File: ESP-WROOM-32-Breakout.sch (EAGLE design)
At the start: 10 parts, among them SW1 PROG, SW2 RST, U3 ESP-WROOM-32

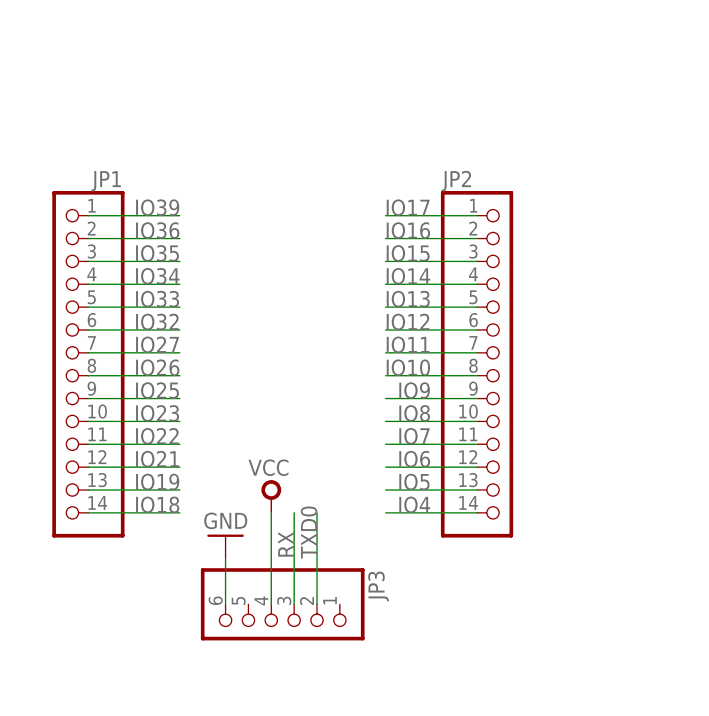
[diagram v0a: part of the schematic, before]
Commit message: smaller header pads reduced board size added mounting holes stitching via’s at antenna
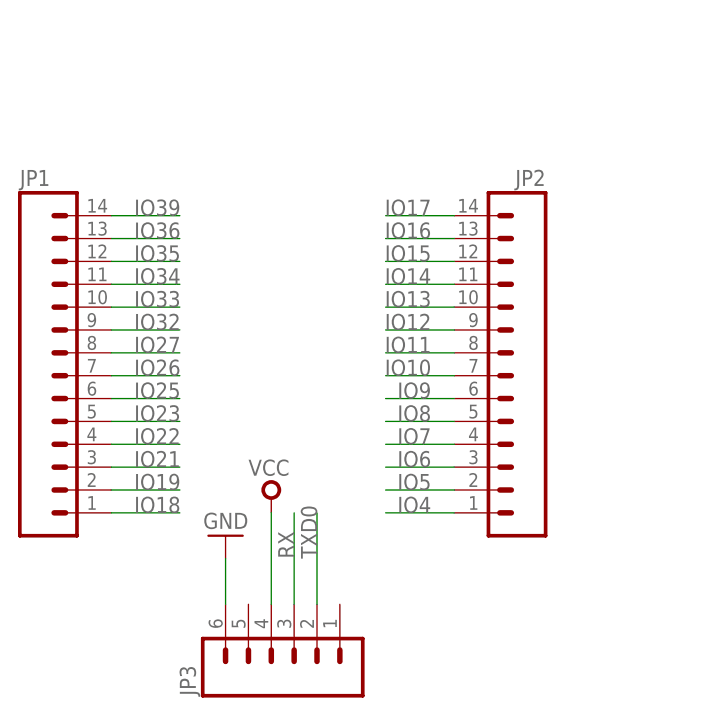
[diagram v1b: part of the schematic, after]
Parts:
- JP1, JP2: device pinhead:PINHD-1X14 -> SparkFun-Connectors:M14
- JP3: device pinhead:PINHD-1X6 -> SparkFun-Connectors:M06SILK_FEMALE_PTH
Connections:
- net IO10: now also JP2.7; no longer JP2.8
- net IO11: now also JP2.8; no longer JP2.7
- net IO12: now also JP2.9; no longer JP2.6
- net IO13: now also JP2.10; no longer JP2.5
- net IO14: now also JP2.11; no longer JP2.4
- net IO15: now also JP2.12; no longer JP2.3
- net IO16: now also JP2.13; no longer JP2.2
- net IO17: now also JP2.14; no longer JP2.1
- net IO18: now also JP1.1; no longer JP1.14
- net IO19: now also JP1.2; no longer JP1.13
- net IO21: now also JP1.3; no longer JP1.12
- net IO22: now also JP1.4; no longer JP1.11
- net IO23: now also JP1.5; no longer JP1.10
- net IO25: now also JP1.6; no longer JP1.9
- net IO26: now also JP1.7; no longer JP1.8
- net IO27: now also JP1.8; no longer JP1.7
- net IO32: now also JP1.9; no longer JP1.6
- net IO33: now also JP1.10; no longer JP1.5
- net IO34: now also JP1.11; no longer JP1.4
- net IO35: now also JP1.12; no longer JP1.3
- net IO36: now also JP1.13; no longer JP1.2
- net IO39: now also JP1.14; no longer JP1.1
- net IO4: now also JP2.1; no longer JP2.14
- net IO5: now also JP2.2; no longer JP2.13
- net IO6: now also JP2.3; no longer JP2.12
- net IO7: now also JP2.4; no longer JP2.11
- net IO8: now also JP2.5; no longer JP2.10
- net IO9: now also JP2.6; no longer JP2.9

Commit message: added reverse-voltage protection
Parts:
- added Q1: 2N7002, nxp_60_1_1:2N7002E
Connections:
- new net GND_IN: JP3.6, Q1.D
- net GND: now also Q1.S; no longer JP3.6
- net VCC: now also Q1.G
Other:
- note added: "PROTECTION"
- note added: "REVERSE VOLTAGE"
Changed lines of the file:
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@@
 <part name="GND1" library="SparkFun-Aesthetics" deviceset="GND" device=""/>
 <part name="FRAME1" library="frames" deviceset="DINA4_L" device=""/>
-<part name="GND6" library="SparkFun-Aesthetics" deviceset="GND" device=""/>
 <part name="V2" library="supply" deviceset="VCC" device=""/>
 <part name="SW1" library="Seeed-OPL-Switch" deviceset="SMD-BUTTON(2P-6.0X3.0X2.5MM)" device="-DHT-1163S" value="PROG"/>
@@
 <part name="JP2" library="SparkFun-Connectors" deviceset="M14" device=""/>
 <part name="JP3" library="SparkFun-Connectors" deviceset="M06" device="SILK_FEMALE_PTH"/>
+<part name="GND34" library="supply1" deviceset="GND" device=""/>
+<part name="Q1" library="nxp_60_1_1" deviceset="2N7002" device="" technology="E" value="2N7002"/>
+<part name="V4" library="supply" deviceset="VCC" device=""/>
 </parts>
 <sheets>
 <sheet>
 <plain>
+<text x="198.12" y="139.7" size="1.778" layer="97">REVERSE VOLTAGE</text>
+<text x="198.12" y="137.16" size="1.778" layer="97">PROTECTION</text>
 </plain>
 <instances>
@@
 <instance part="FRAME1" gate="G$1" x="0" y="0"/>
 <instance part="FRAME1" gate="G$2" x="162.56" y="0"/>
-<instance part="GND6" gate="1" x="45.72" y="38.1" rot="R180"/>
 <instance part="V2" gate="VCC" x="50.8" y="43.18"/>
 <instance part="SW1" gate="G$1" x="38.1" y="127" rot="R90"/>
@@
 <instance part="JP2" gate="G$1" x="81.28" y="58.42" rot="MR0"/>
 <instance part="JP3" gate="G$1" x="53.34" y="25.4" rot="R90"/>
+<instance part="GND34" gate="1" x="193.04" y="134.62"/>
+<instance part="Q1" gate="G$1" x="195.58" y="149.86" rot="MR0"/>
+<instance part="V4" gate="VCC" x="213.36" y="149.86"/>
 </instances>
 <busses>
@@
 </segment>
 <segment>
-<wire x1="45.72" y1="30.48" x2="45.72" y2="35.56" width="0.1524" layer="91"/>
-<pinref part="GND6" gate="1" pin="GND"/>
-<pinref part="JP3" gate="G$1" pin="6"/>
-</segment>
-<segment>
 <pinref part="GND1" gate="1" pin="GND"/>
 <pinref part="SW1" gate="G$1" pin="1"/>
@@
 <pinref part="GND5" gate="1" pin="GND"/>
 <pinref part="SW2" gate="G$1" pin="1"/>
+</segment>
+<segment>
+<pinref part="GND34" gate="1" pin="GND"/>
+<pinref part="Q1" gate="G$1" pin="S"/>
+<wire x1="193.04" y1="137.16" x2="193.04" y2="144.78" width="0.1524" layer="91"/>
 </segment>
 </net>
@@
 <pinref part="V2" gate="VCC" pin="VCC"/>
 <pinref part="JP3" gate="G$1" pin="4"/>
+</segment>
+<segment>
+<pinref part="Q1" gate="G$1" pin="G"/>
+<wire x1="213.36" y1="147.32" x2="198.12" y2="147.32" width="0.1524" layer="91"/>
+<pinref part="V4" gate="VCC" pin="VCC"/>
 </segment>
 </net>
@@
 </segment>
 </net>
+<net name="GND_IN" class="1">
+<segment>
+<wire x1="45.72" y1="30.48" x2="45.72" y2="35.56" width="0.1524" layer="91"/>
+<pinref part="JP3" gate="G$1" pin="6"/>
+<label x="45.72" y="33.02" size="1.778" layer="95" rot="R90"/>
+</segment>
+<segment>
+<pinref part="Q1" gate="G$1" pin="D"/>
+<wire x1="193.04" y1="165.1" x2="193.04" y2="154.94" width="0.1524" layer="91"/>
+<label x="193.04" y="157.48" size="1.778" layer="95" rot="R90"/>
+</segment>
+</net>

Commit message: changed diode package to SOD-323
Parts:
- D1: device Seeed-OPL-Diode:DIODE'1N4148-SMD' -> Seeed-OPL-Diode:DIODE'0805'
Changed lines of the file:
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@@
 <part name="SW1" library="Seeed-OPL-Switch" deviceset="SMD-BUTTON(2P-6.0X3.0X2.5MM)" device="-DHT-1163S" value="PROG"/>
 <part name="SW2" library="Seeed-OPL-Switch" deviceset="SMD-BUTTON(2P-6.0X3.0X2.5MM)" device="-DHT-1163S" value="RST"/>
-<part name="D1" library="Seeed-OPL-Diode" deviceset="DIODE*" device="'1N4148-SMD'"/>
+<part name="D1" library="Seeed-OPL-Diode" deviceset="DIODE*" device="'0805'"/>
 <part name="JP1" library="SparkFun-Connectors" deviceset="M14" device=""/>
 <part name="JP2" library="SparkFun-Connectors" deviceset="M14" device=""/>
